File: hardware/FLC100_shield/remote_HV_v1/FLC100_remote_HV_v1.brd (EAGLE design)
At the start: 49.5 x 49.5 mm, 25 parts, among them IC1 MCP3424, IC3 LM1702-5V, X1 RJ11-6P6CPTH

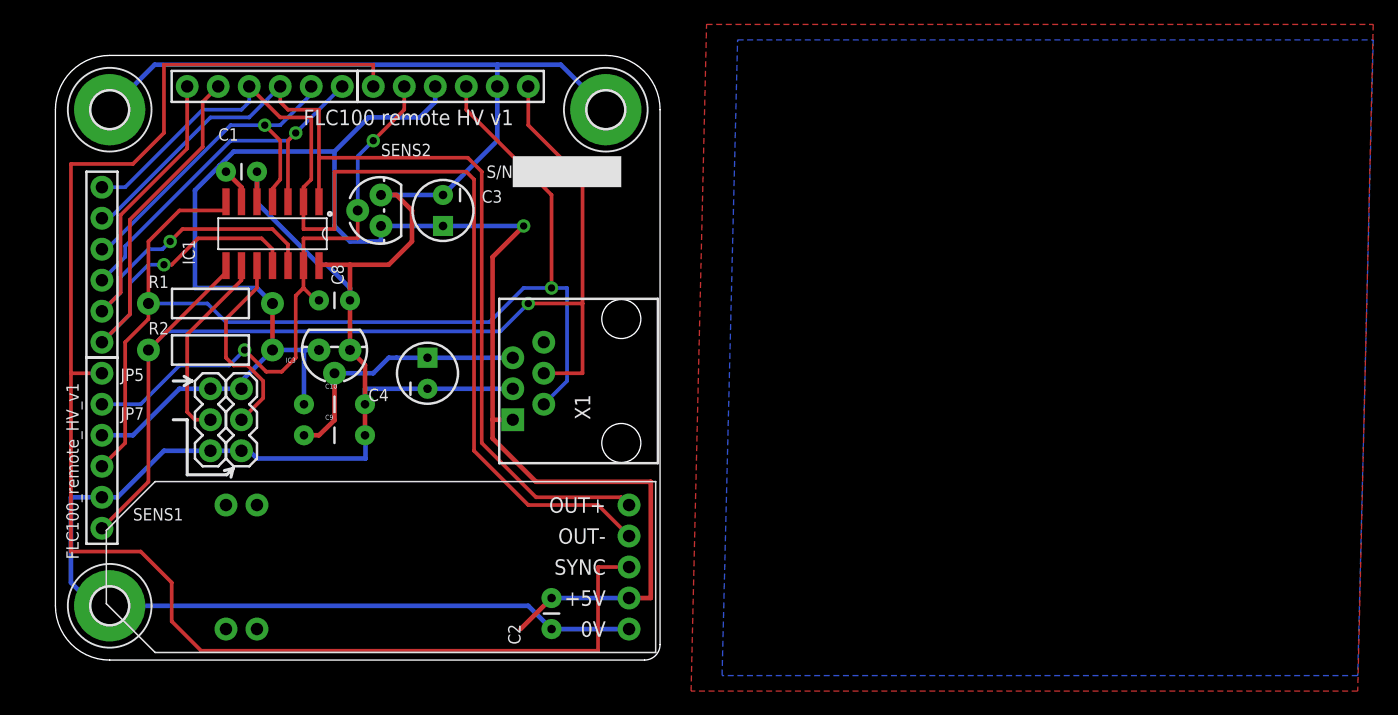
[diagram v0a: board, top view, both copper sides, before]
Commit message: Updated MCP3424 footprint for easier hand soldering.
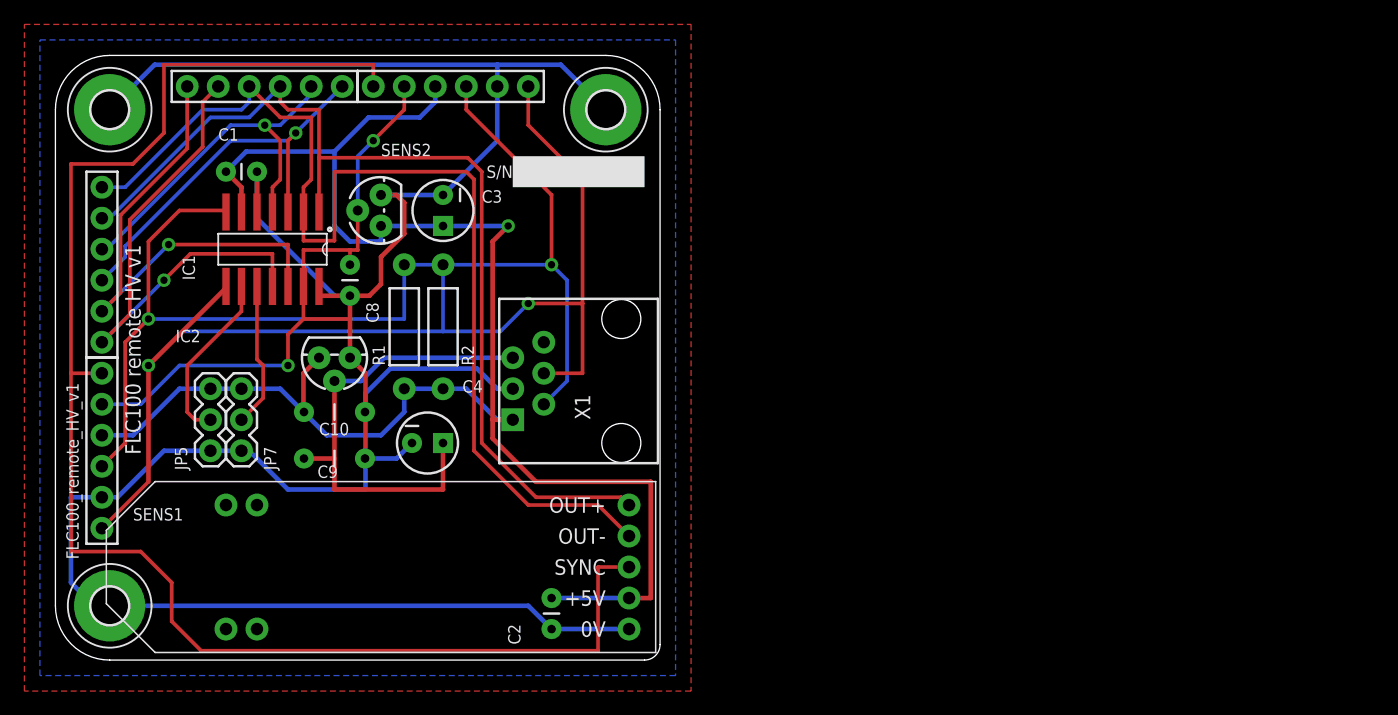
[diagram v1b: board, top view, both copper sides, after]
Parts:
- removed IC3: LM1702-5V, SteveMarple:TO-92@2
- added IC2: LM1702-5V, SteveMarple:TO-92@2
- IC1: device SteveMarple:SO14 -> SteveMarple:SO14-HAND
- moved R2 19.1 mm to (31.8, 27.3), turned to 270 degrees
- moved R1 16.0 mm to (28.6, 27.3), turned to 270 degrees
- moved C4 5.71 mm to (30.5, 17.8), turned to 0 degrees
- moved C8 3.87 mm to (24.1, 32.4), turned to 270 degrees
- moved C9 1.90 mm to (22.9, 16.5)
- moved IC1 1.27 mm to (17.8, 33.7)
- moved C10 0.63 mm to (22.9, 20.3)
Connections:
- net N$11 renamed ADDR0
- net N$12 renamed ADDR1
- net +5V: now also IC2.3; no longer IC3.3
- net GND: now also IC2.1; no longer IC3.1
- net VIN: now also IC2.2; no longer IC3.2
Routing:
- net VIN: track 22.0 -> 39.5 mm
- net GND: track 201.9 -> 212.0 mm
- net +5V: track 151.0 -> 143.9 mm
- net ADDR1: track 16.3 -> 11.9 mm
- net SCL: track 91.4 -> 95.7 mm, vias 1 -> 2
- net CH1-: track 88.5 -> 90.4 mm
- net TEMP: track 49.1 -> 51.0 mm
- net ADDR0: track 16.0 -> 14.3 mm
- net SDA: track 93.9 -> 95.2 mm, vias 1 -> 2
- net CH3+: track 45.6 -> 44.5 mm
- net CH2-: track 30.1 -> 30.9 mm
- net CH2+: track 32.7 -> 33.5 mm
- net CH1+: track 81.5 -> 82.4 mm
